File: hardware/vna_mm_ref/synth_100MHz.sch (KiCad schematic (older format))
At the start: 27 parts, among them U301 HMC1031, X301 ABLNO-V-100.000MHZ

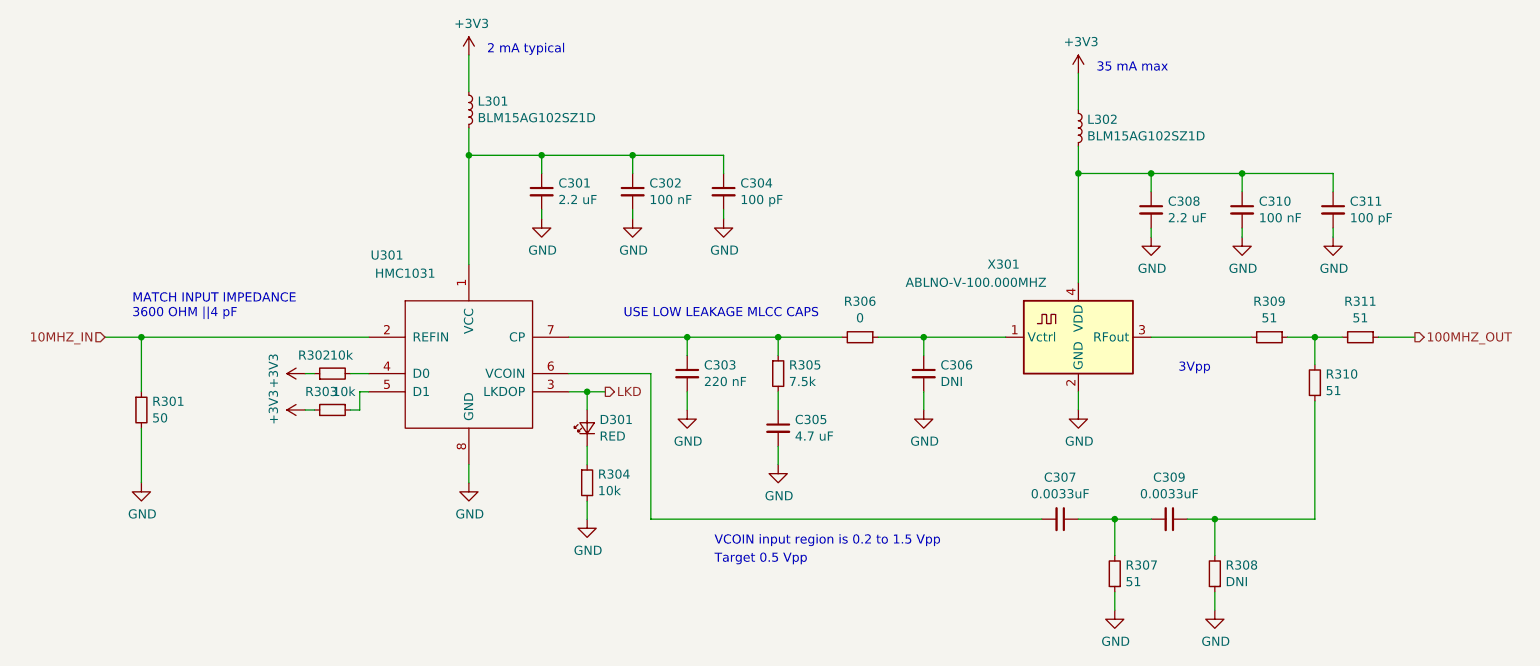
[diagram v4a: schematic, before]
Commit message: component placement on vna ref board
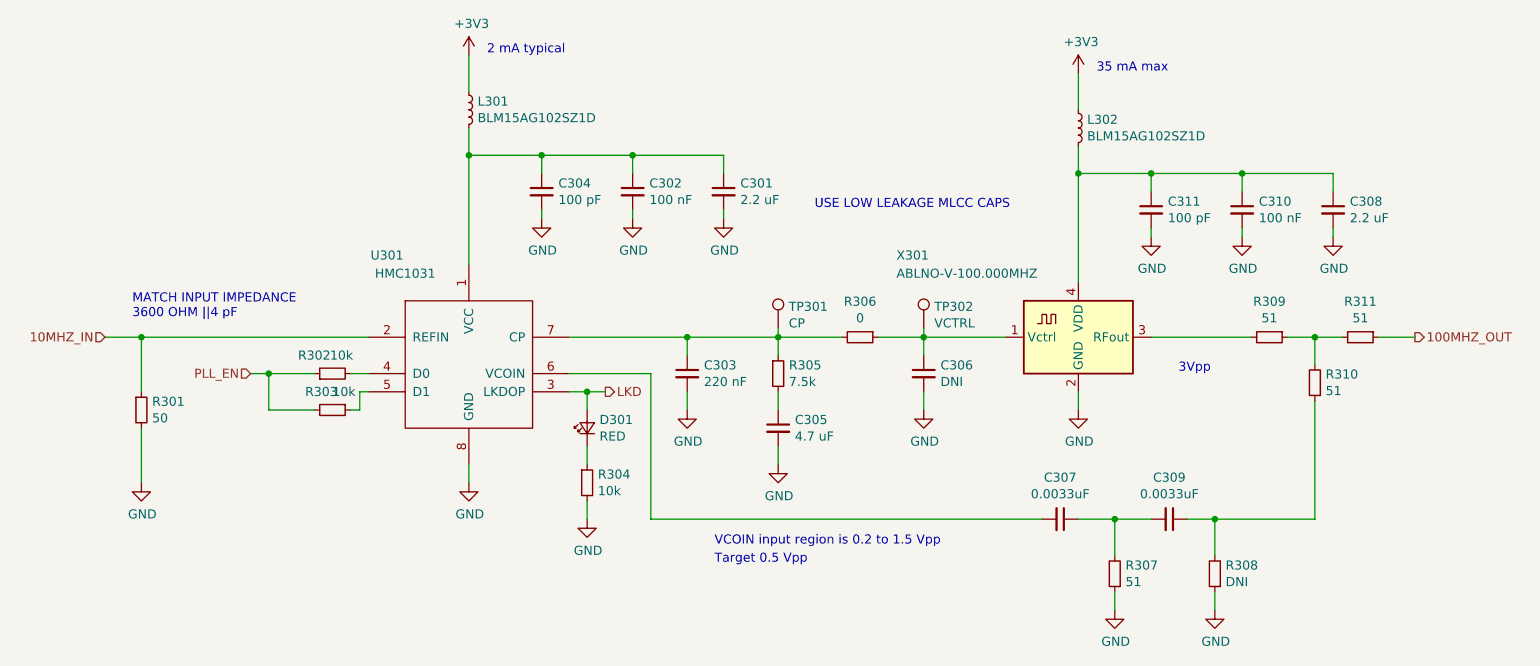
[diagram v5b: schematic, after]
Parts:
- added TP301: CP, TestPoint:TestPoint_Keystone_5015_Micro-Minature, symbol Connector:TestPoint
- added TP302: VCTRL, TestPoint:TestPoint_Keystone_5015_Micro-Minature, symbol Connector:TestPoint
- U301: footprint Housings_SSOP:MSOP-8_3x3mm_Pitch0.65mm -> Package_SO:MSOP-8_3x3mm_P0.65mm
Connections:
- net +3V3: no longer R302.1, R303.2
- net at C303.1, R305.1, R306.2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: now also TP301.1
- net at C306.1, R306.1, X301.1 (Vctrl): now also TP302.1
- new net PLL_EN: R302.1, R303.2
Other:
- moved on the sheet: C301, C304, C308, C311
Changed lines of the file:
@@
 	3700 4300 3700 4400
-$Comp
-L Oscillator:ABLNO X?
-U 1 1 5DC2749C
-P 7050 3600
-AR Path="/5DC2749C" Ref="X?"  Part="1"
-AR Path="/5DC1A65E/5DC2749C" Ref="X301"  Part="1"
-F 0 "X301" H 6550 4000 50  0000 L CNN
-F 1 "ABLNO-V-100.000MHZ" H 6100 3900 50  0000 L CNN
-F 2 "Oscillator:Oscillator_SMD_Abracon_ABLNO" H 7050 3250 50  0001 C CNN
-F 3 "https://abracon.com/Precisiontiming/ABLNO.pdf" H 6850 3700 50  0001 C CNN
-	1    7050 3600
-	1    0    0    -1
-$EndComp
 $Comp
 L power:GND #PWR?
@@
 	0    -1   -1   0
 $EndComp
-Text Notes 4550 3500 0    50   ~ 0
+Text Notes 5600 2900 0    50   ~ 0
 USE LOW LEAKAGE MLCC CAPS
 $Comp
@@
 L Device:C_Small C?
 U 1 1 5DC27520
-P 5100 2800
+P 4100 2800
 AR Path="/5DC27520" Ref="C?"  Part="1"
 AR Path="/5DC1A65E/5DC27520" Ref="C304"  Part="1"
-F 0 "C304" H 5192 2846 50  0000 L CNN
-F 1 "100 pF" H 5192 2755 50  0000 L CNN
-F 2 "Capacitor_SMD:C_0402_1005Metric" H 5100 2800 50  0001 C CNN
-F 3 "~" H 5100 2800 50  0001 C CNN
-	1    5100 2800
+F 0 "C304" H 4192 2846 50  0000 L CNN
+F 1 "100 pF" H 4192 2755 50  0000 L CNN
+F 2 "Capacitor_SMD:C_0402_1005Metric" H 4100 2800 50  0001 C CNN
+F 3 "~" H 4100 2800 50  0001 C CNN
+	1    4100 2800
 	1    0    0    -1
 $EndComp
@@
 L Device:C_Small C?
 U 1 1 5DC2752C
-P 4100 2800
+P 5100 2800
 AR Path="/5DC2752C" Ref="C?"  Part="1"
 AR Path="/5DC1A65E/5DC2752C" Ref="C301"  Part="1"
-F 0 "C301" H 4192 2846 50  0000 L CNN
-F 1 "2.2 uF" H 4192 2755 50  0000 L CNN
-F 2 "Capacitor_SMD:C_0603_1608Metric" H 4100 2800 50  0001 C CNN
-F 3 "~" H 4100 2800 50  0001 C CNN
-	1    4100 2800
+F 0 "C301" H 5192 2846 50  0000 L CNN
+F 1 "2.2 uF" H 5192 2755 50  0000 L CNN
+F 2 "Capacitor_SMD:C_0603_1608Metric" H 5100 2800 50  0001 C CNN
+F 3 "~" H 5100 2800 50  0001 C CNN
+	1    5100 2800
 	1    0    0    -1
 $EndComp
@@
 L Device:C_Small C?
 U 1 1 5DC27560
-P 8450 2900
+P 7450 2900
 AR Path="/5DC27560" Ref="C?"  Part="1"
 AR Path="/5DC1A65E/5DC27560" Ref="C311"  Part="1"
-F 0 "C311" H 8542 2946 50  0000 L CNN
-F 1 "100 pF" H 8542 2855 50  0000 L CNN
-F 2 "Capacitor_SMD:C_0402_1005Metric" H 8450 2900 50  0001 C CNN
-F 3 "~" H 8450 2900 50  0001 C CNN
-	1    8450 2900
+F 0 "C311" H 7542 2946 50  0000 L CNN
+F 1 "100 pF" H 7542 2855 50  0000 L CNN
+F 2 "Capacitor_SMD:C_0402_1005Metric" H 7450 2900 50  0001 C CNN
+F 3 "~" H 7450 2900 50  0001 C CNN
+	1    7450 2900
 	1    0    0    -1
 $EndComp
@@
 L Device:C_Small C?
 U 1 1 5DC2756C
-P 7450 2900
+P 8450 2900
 AR Path="/5DC2756C" Ref="C?"  Part="1"
 AR Path="/5DC1A65E/5DC2756C" Ref="C308"  Part="1"
-F 0 "C308" H 7542 2946 50  0000 L CNN
-F 1 "2.2 uF" H 7542 2855 50  0000 L CNN
-F 2 "Capacitor_SMD:C_0603_1608Metric" H 7450 2900 50  0001 C CNN
-F 3 "~" H 7450 2900 50  0001 C CNN
-	1    7450 2900
+F 0 "C308" H 8542 2946 50  0000 L CNN
+F 1 "2.2 uF" H 8542 2855 50  0000 L CNN
+F 2 "Capacitor_SMD:C_0603_1608Metric" H 8450 2900 50  0001 C CNN
+F 3 "~" H 8450 2900 50  0001 C CNN
+	1    8450 2900
 	1    0    0    -1
 $EndComp
@@
 F 0 "U301" H 3250 4250 50  0000 C CNN
 F 1 "HMC1031" H 3350 4150 50  0000 C CNN
-F 2 "Housings_SSOP:MSOP-8_3x3mm_Pitch0.65mm" H 2700 4300 50  0001 C CNN
+F 2 "Package_SO:MSOP-8_3x3mm_P0.65mm" H 2700 4300 50  0001 C CNN
 F 3 "https://www.analog.com/media/en/technical-documentation/data-sheets/hmc1031.pdf" H 3650 4600 50  0001 C CNN
 	1    3700 3700
@@
 Text Notes 5050 4750 0    50   ~ 0
 VCOIN input region is 0.2 to 1.5 Vpp
-$Comp
-L power:+3V3 #PWR?
-U 1 1 5DED131B
-P 2800 4000
-AR Path="/5DED131B" Ref="#PWR?"  Part="1"
-AR Path="/5DC1A65E/5DED131B" Ref="#PWR0303"  Part="1"
-F 0 "#PWR0303" H 2800 3850 50  0001 C CNN
-F 1 "+3V3" H 2815 4173 50  0000 C CNN
-F 2 "" H 2800 4000 50  0001 C CNN
-F 3 "" H 2800 4000 50  0001 C CNN
-	1    2800 4000
-	0    -1   -1   0
-$EndComp
 $Comp
 L Device:R_Small R?
@@
 $EndComp
 Wire Wire Line
-	2850 4000 2800 4000
-$Comp
-L power:+3V3 #PWR?
-U 1 1 5DED581B
-P 2800 3800
-AR Path="/5DED581B" Ref="#PWR?"  Part="1"
-AR Path="/5DC1A65E/5DED581B" Ref="#PWR0302"  Part="1"
-F 0 "#PWR0302" H 2800 3650 50  0001 C CNN
-F 1 "+3V3" H 2815 3973 50  0000 C CNN
-F 2 "" H 2800 3800 50  0001 C CNN
-F 3 "" H 2800 3800 50  0001 C CNN
-	1    2800 3800
-	0    -1   -1   0
-$EndComp
-Wire Wire Line
-	2800 3800 2850 3800
-Wire Wire Line
 	3050 4000 3100 4000
 Wire Wire Line
@@
 Wire Wire Line
 	7450 3600 8000 3600
+Wire Wire Line
+	2600 3800 2600 4000
+Wire Wire Line
+	2600 4000 2850 4000
+Wire Wire Line
+	2600 3800 2850 3800
+Wire Wire Line
+	2600 3800 2500 3800
+Connection ~ 2600 3800
+Text HLabel 2500 3800 0    50   Input ~ 0
+PLL_EN
+$Comp
+L Connector:TestPoint TP?
+U 1 1 5DF116B9
+P 6200 3550
+AR Path="/5DC45DA8/5DF116B9" Ref="TP?"  Part="1"
+AR Path="/5DC1A65E/5DF116B9" Ref="TP302"  Part="1"
+F 0 "TP302" H 6258 3668 50  0000 L CNN
+F 1 "VCTRL" H 6258 3577 50  0000 L CNN
+F 2 "TestPoint:TestPoint_Keystone_5015_Micro-Minature" H 6400 3550 50  0001 C CNN
+F 3 "~" H 6400 3550 50  0001 C CNN
+	1    6200 3550
+	1    0    0    -1
+$EndComp
+$Comp
+L Connector:TestPoint TP?
+U 1 1 5DF12DC8
+P 5400 3550
+AR Path="/5DC45DA8/5DF12DC8" Ref="TP?"  Part="1"
+AR Path="/5DC1A65E/5DF12DC8" Ref="TP301"  Part="1"
+F 0 "TP301" H 5458 3668 50  0000 L CNN
+F 1 "CP" H 5458 3577 50  0000 L CNN
+F 2 "TestPoint:TestPoint_Keystone_5015_Micro-Minature" H 5600 3550 50  0001 C CNN
+F 3 "~" H 5600 3550 50  0001 C CNN
+	1    5400 3550
+	1    0    0    -1
+$EndComp
+$Comp
+L Oscillator:ABLNO X?
+U 1 1 5DC2749C
+P 7050 3600
+AR Path="/5DC2749C" Ref="X?"  Part="1"
+AR Path="/5DC1A65E/5DC2749C" Ref="X301"  Part="1"
+F 0 "X301" H 6050 4050 50  0000 L CNN
+F 1 "ABLNO-V-100.000MHZ" H 6050 3950 50  0000 L CNN
+F 2 "Oscillator:Oscillator_SMD_Abracon_ABLNO" H 7050 3250 50  0001 C CNN
+F 3 "https://abracon.com/Precisiontiming/ABLNO.pdf" H 6850 3700 50  0001 C CNN
+	1    7050 3600
+	1    0    0    -1
+$EndComp
+Wire Wire Line
+	5400 3550 5400 3600
+Wire Wire Line
+	6200 3550 6200 3600
 $EndSCHEMATC

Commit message: layout of 100 MHz reference board
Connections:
- net PLL_EN is gone; now on net +3V3: R302.1, R303.2
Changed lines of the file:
@@
 	2600 3800 2500 3800
 Connection ~ 2600 3800
-Text HLabel 2500 3800 0    50   Input ~ 0
-PLL_EN
 $Comp
 L Connector:TestPoint TP?
@@
 Wire Wire Line
 	6200 3550 6200 3600
+$Comp
+L power:+3V3 #PWR?
+U 1 1 5DF96849
+P 2500 3800
+AR Path="/5DF96849" Ref="#PWR?"  Part="1"
+AR Path="/5DC1A65E/5DF96849" Ref="#PWR0121"  Part="1"
+F 0 "#PWR0121" H 2500 3650 50  0001 C CNN
+F 1 "+3V3" H 2515 3973 50  0000 C CNN
+F 2 "" H 2500 3800 50  0001 C CNN
+F 3 "" H 2500 3800 50  0001 C CNN
+	1    2500 3800
+	0    -1   -1   0
+$EndComp
 $EndSCHEMATC

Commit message: created BOM for vna mm ref
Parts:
- C301, C308: DIST_NAME (none) -> Digi-Key; DIST_PN (none) -> 490-10731-1-ND
- C305: DIST_NAME (none) -> Digi-Key; DIST_PN (none) -> 445-14258-1-ND
- L301, L302: DIST_NAME (none) -> Digi-Key; DIST_PN (none) -> BLM15AG102SZ1D
- TP301, TP302: DIST_NAME (none) -> Digi-Key; DIST_PN (none) -> 36-5015CT-ND
- U301: DIST_NAME (none) -> Digi-Key; DIST_PN (none) -> HMC1031MS8ETR
- X301: DIST_NAME (none) -> Digi-Key; DIST_PN (none) -> 535-12341-1-ND
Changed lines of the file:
@@
 F 2 "Capacitor_SMD:C_0603_1608Metric" H 5400 4100 50  0001 C CNN
 F 3 "~" H 5400 4100 50  0001 C CNN
+F 4 "Digi-Key" H 5400 4100 50  0001 C CNN "DIST_NAME"
+F 5 "445-14258-1-ND" H 5400 4100 50  0001 C CNN "DIST_PN"
 	1    5400 4100
 	1    0    0    -1
@@
 F 2 "Inductor_SMD:L_0402_1005Metric" H 3700 2350 50  0001 C CNN
 F 3 "~" H 3700 2350 50  0001 C CNN
+F 4 "Digi-Key" H 3700 2350 50  0001 C CNN "DIST_NAME"
+F 5 "BLM15AG102SZ1D" H 3700 2350 50  0001 C CNN "DIST_PN"
 	1    3700 2350
 	1    0    0    -1
@@
 F 2 "Capacitor_SMD:C_0603_1608Metric" H 5100 2800 50  0001 C CNN
 F 3 "~" H 5100 2800 50  0001 C CNN
+F 4 "Digi-Key" H 5100 2800 50  0001 C CNN "DIST_NAME"
+F 5 "490-10731-1-ND" H 5100 2800 50  0001 C CNN "DIST_PN"
 	1    5100 2800
 	1    0    0    -1
@@
 F 2 "Inductor_SMD:L_0402_1005Metric" H 7050 2450 50  0001 C CNN
 F 3 "~" H 7050 2450 50  0001 C CNN
+F 4 "Digi-Key" H 7050 2450 50  0001 C CNN "DIST_NAME"
+F 5 "BLM15AG102SZ1D" H 7050 2450 50  0001 C CNN "DIST_PN"
 	1    7050 2450
 	1    0    0    -1
@@
 F 2 "Capacitor_SMD:C_0603_1608Metric" H 8450 2900 50  0001 C CNN
 F 3 "~" H 8450 2900 50  0001 C CNN
+F 4 "Digi-Key" H 8450 2900 50  0001 C CNN "DIST_NAME"
+F 5 "490-10731-1-ND" H 8450 2900 50  0001 C CNN "DIST_PN"
 	1    8450 2900
 	1    0    0    -1
@@
 F 2 "Package_SO:MSOP-8_3x3mm_P0.65mm" H 2700 4300 50  0001 C CNN
 F 3 "https://www.analog.com/media/en/technical-documentation/data-sheets/hmc1031.pdf" H 3650 4600 50  0001 C CNN
+F 4 "Digi-Key" H 3700 3700 50  0001 C CNN "DIST_NAME"
+F 5 "HMC1031MS8ETR" H 3700 3700 50  0001 C CNN "DIST_PN"
 	1    3700 3700
 	1    0    0    -1
@@
 F 2 "TestPoint:TestPoint_Keystone_5015_Micro-Minature" H 6400 3550 50  0001 C CNN
 F 3 "~" H 6400 3550 50  0001 C CNN
+F 4 "Digi-Key" H 6200 3550 50  0001 C CNN "DIST_NAME"
+F 5 "36-5015CT-ND" H 6200 3550 50  0001 C CNN "DIST_PN"
 	1    6200 3550
 	1    0    0    -1
@@
 F 2 "TestPoint:TestPoint_Keystone_5015_Micro-Minature" H 5600 3550 50  0001 C CNN
 F 3 "~" H 5600 3550 50  0001 C CNN
+F 4 "Digi-Key" H 5400 3550 50  0001 C CNN "DIST_NAME"
+F 5 "36-5015CT-ND" H 5400 3550 50  0001 C CNN "DIST_PN"
 	1    5400 3550
 	1    0    0    -1
@@
 F 2 "Oscillator:Oscillator_SMD_Abracon_ABLNO" H 7050 3250 50  0001 C CNN
 F 3 "https://abracon.com/Precisiontiming/ABLNO.pdf" H 6850 3700 50  0001 C CNN
+F 4 "535-12341-1-ND" H 7050 3600 50  0001 C CNN "DIST_PN"
+F 5 "Digi-Key" H 7050 3600 50  0001 C CNN "DIST_NAME"
 	1    7050 3600
 	1    0    0    -1

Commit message: AC couple HMC1031 input on ref board
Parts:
- R301: value 50 -> DNI
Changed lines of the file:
@@
 AR Path="/5DC1A65E/5DB93EC3" Ref="R301"  Part="1"
 F 0 "R301" H 1959 4046 50  0000 L CNN
-F 1 "50" H 1959 3955 50  0000 L CNN
+F 1 "DNI" H 1959 3955 50  0000 L CNN
 F 2 "Resistor_SMD:R_0402_1005Metric" H 1900 4000 50  0001 C CNN
 F 3 "~" H 1900 4000 50  0001 C CNN
